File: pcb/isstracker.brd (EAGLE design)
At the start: 68.6 x 54.3 mm, 24 parts, among them IC2 L7805CV, J1 MOTOR_RIGHT, J2 MOTOR, J3 MOTOR_LEFT, J4 DISPLAY, J6 CONTROL, J8 UART, J9 DISTANCE, Q2 60V/32A/35mΩ, U1 ARGON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

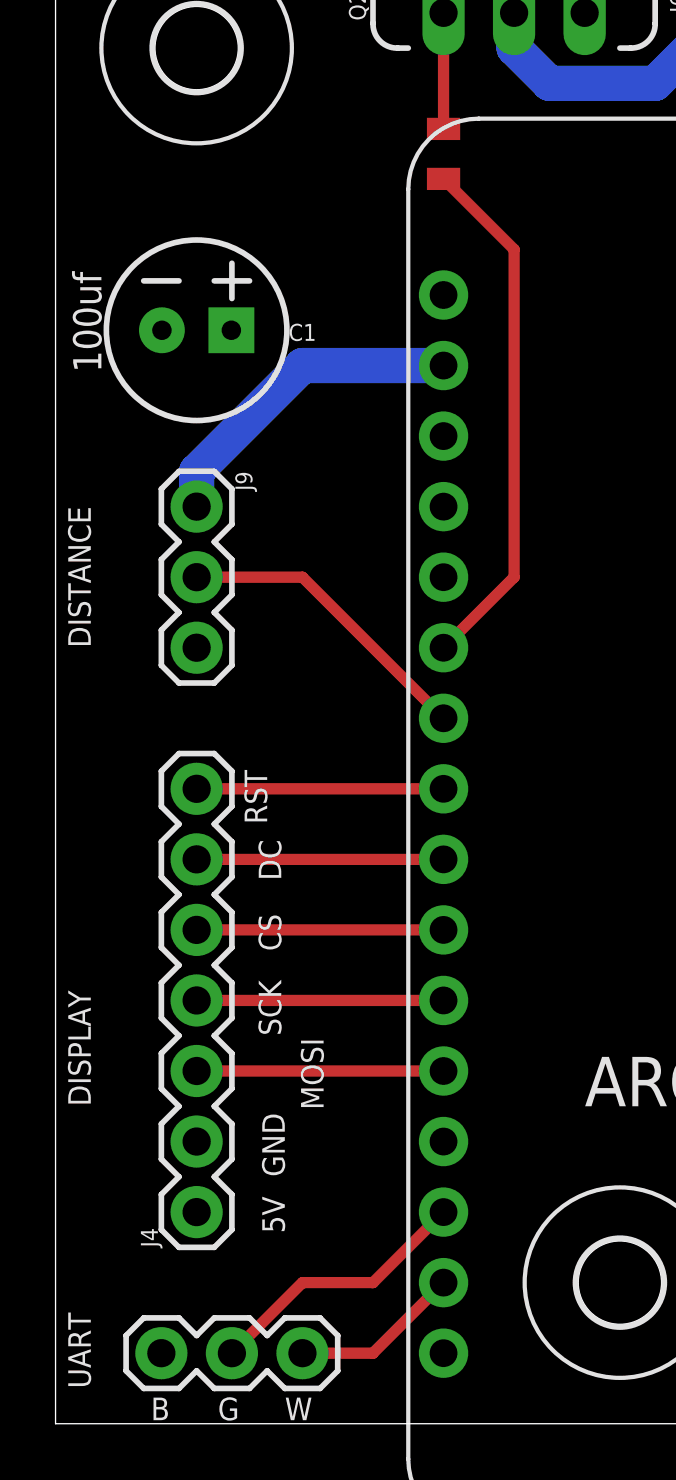
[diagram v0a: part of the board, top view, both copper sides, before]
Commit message: Control board version 1.7
* Added a pushbutton to turn the globe back on
* Began to put globe power control back into app
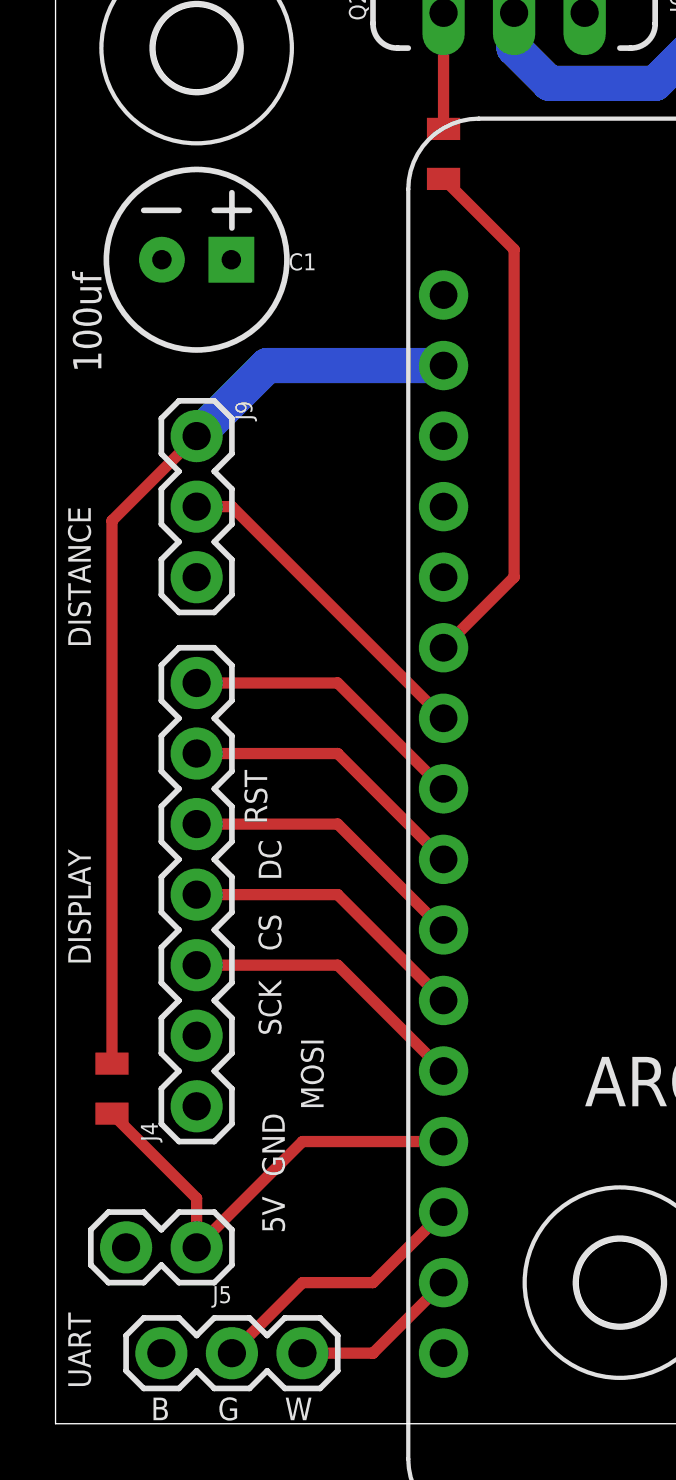
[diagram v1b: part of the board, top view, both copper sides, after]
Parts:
- added J5: GLOBE_RESET, SparkFun-Connectors:1X02
- added R4: 10k, SparkFun-Resistors:0805
- moved J4 3.81 mm to (5.08, 11.4)
- moved C1 2.54 mm to (5.08, 41.9)
- moved J9 2.54 mm to (5.08, 35.6)
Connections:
- new net MISO: J5.1, R4.2, U1.13
- net +3V3: now also R4.1
- net GND: now also J5.2
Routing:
- net +3V3: track 11.7 -> 33.8 mm
- net MISO: track 0.00 -> 16.5 mm
- net SCK: track 8.89 -> 10.5 mm
- net RST: track 8.89 -> 10.5 mm
- net MOSI: track 8.89 -> 10.5 mm
- net DC: track 8.89 -> 10.5 mm
- net CS: track 8.89 -> 10.5 mm
- net DISTANCE: track 11.0 -> 12.0 mm
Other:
- board text added: "ISS Position Tracker (C) Peter Buelow March, 2021 Version 1.7"
- board text removed: "ISS Position Tracker (C) Peter Buelow March, 2021 Version 1.6"
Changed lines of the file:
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@@
 <wire x1="68.56" y1="54.28" x2="0" y2="54.28" width="0" layer="20"/>
 <wire x1="0" y1="54.28" x2="0" y2="0" width="0" layer="20"/>
-<text x="1.27" y="11.43" size="0.8128" layer="121" rot="R90">DISPLAY</text>
+<text x="1.27" y="16.51" size="0.8128" layer="121" rot="R90">DISPLAY</text>
 <text x="33.147" y="48.514" size="0.8128" layer="121" rot="R180">CONTROL</text>
 <text x="27.686" y="53.721" size="0.6096" layer="121" rot="R180">GND</text>
@@
 (C) Peter Buelow
 March, 2021
-Version 1.6</text>
+Version 1.7</text>
 <text x="3.429" y="0.127" size="0.8128" layer="121">B</text>
 <text x="52.07" y="5.08" size="0.6096" layer="121">LM7805</text>
@@
 <attribute name="VALUE" x="52.578" y="49.53" size="0.6096" layer="27" font="vector" ratio="20" rot="R270"/>
 </element>
-<element name="J4" library="SparkFun-Connectors" library_urn="urn:adsk.eagle:library:513" package="1X07" package3d_urn="urn:adsk.eagle:package:38129/1" value="DISPLAY" x="5.08" y="7.62" smashed="yes" rot="R90">
-<attribute name="NAME" x="3.683" y="6.35" size="0.6096" layer="25" font="vector" ratio="20" rot="R90"/>
-</element>
-<element name="J9" library="SparkFun-Connectors" library_urn="urn:adsk.eagle:library:513" package="1X03" package3d_urn="urn:adsk.eagle:package:38063/1" value="DISTANCE" x="5.08" y="33.02" smashed="yes" rot="R270">
-<attribute name="NAME" x="6.477" y="34.29" size="0.6096" layer="25" font="vector" ratio="20" rot="R270"/>
+<element name="J4" library="SparkFun-Connectors" library_urn="urn:adsk.eagle:library:513" package="1X07" package3d_urn="urn:adsk.eagle:package:38129/1" value="DISPLAY" x="5.08" y="11.43" smashed="yes" rot="R90">
+<attribute name="NAME" x="3.683" y="10.16" size="0.6096" layer="25" font="vector" ratio="20" rot="R90"/>
+</element>
+<element name="J9" library="SparkFun-Connectors" library_urn="urn:adsk.eagle:library:513" package="1X03" package3d_urn="urn:adsk.eagle:package:38063/1" value="DISTANCE" x="5.08" y="35.56" smashed="yes" rot="R270">
+<attribute name="NAME" x="6.477" y="36.83" size="0.6096" layer="25" font="vector" ratio="20" rot="R270"/>
 </element>
 <element name="D1" library="diode" library_urn="urn:adsk.eagle:library:210" package="DO41-10" package3d_urn="urn:adsk.eagle:package:43336/1" value="1N4004" x="58.293" y="10.922" smashed="yes" rot="R270">
@@
 <attribute name="PROD_ID" value="CAP-08439" x="60.833" y="25.781" size="0.8128" layer="27" rot="R270" display="off"/>
 </element>
-<element name="C1" library="SparkFun-Capacitors" library_urn="urn:adsk.eagle:library:510" package="CPOL-RADIAL-2.5MM-6.5MM" package3d_urn="urn:adsk.eagle:package:37415/1" value="100uF" x="5.08" y="39.37" smashed="yes">
-<attribute name="NAME" x="8.89" y="38.989" size="0.6096" layer="25" font="vector" ratio="20" align="bottom-center"/>
-<attribute name="PROD_ID" value="CAP-08439" x="5.08" y="39.37" size="0.6096" layer="27" display="off"/>
+<element name="C1" library="SparkFun-Capacitors" library_urn="urn:adsk.eagle:library:510" package="CPOL-RADIAL-2.5MM-6.5MM" package3d_urn="urn:adsk.eagle:package:37415/1" value="100uF" x="5.08" y="41.91" smashed="yes">
+<attribute name="NAME" x="8.89" y="41.529" size="0.6096" layer="25" font="vector" ratio="20" align="bottom-center"/>
+<attribute name="PROD_ID" value="CAP-08439" x="5.08" y="41.91" size="0.6096" layer="27" display="off"/>
 </element>
 <element name="J3" library="SparkFun-Connectors" library_urn="urn:adsk.eagle:library:513" package="1X12" package3d_urn="urn:adsk.eagle:package:38169/1" value="MOTOR_LEFT" x="39.37" y="10.16" smashed="yes" rot="R90">
@@
 <element name="LED3" library="adafruit" library_urn="urn:adsk.eagle:library:420" package="CHIPLED_1206" package3d_urn="urn:adsk.eagle:package:6240560/1" value="L171L-LPGC" x="44.45" y="2.54" smashed="yes" rot="R90"/>
 <element name="LED1" library="adafruit" library_urn="urn:adsk.eagle:library:420" package="CHIPLED_1206" package3d_urn="urn:adsk.eagle:package:6240560/1" value="L171L-LPGC" x="35.56" y="48.26" smashed="yes" rot="R180"/>
+<element name="J5" library="SparkFun-Connectors" library_urn="urn:adsk.eagle:library:513" package="1X02" package3d_urn="urn:adsk.eagle:package:38039/1" value="GLOBE_RESET" x="5.08" y="6.35" smashed="yes" rot="R180">
+<attribute name="NAME" x="6.35" y="4.953" size="0.6096" layer="25" font="vector" ratio="20" rot="R180"/>
+<attribute name="VALUE" x="6.35" y="8.382" size="0.6096" layer="27" font="vector" ratio="20" rot="R180"/>
+</element>
+<element name="R4" library="SparkFun-Resistors" library_urn="urn:adsk.eagle:library:532" package="0805" package3d_urn="urn:adsk.eagle:package:39651/1" value="10k" x="2.032" y="12.065" smashed="yes" rot="R270">
+<attribute name="PROD_ID" value="RES-08474" x="2.032" y="12.065" size="0.8128" layer="27" rot="R270" display="off"/>
+<attribute name="VALUE" x="1.143" y="12.065" size="0.6096" layer="27" font="vector" ratio="20" rot="R270" align="top-center"/>
+</element>
 </elements>
 <signals>
@@
 <wire x1="39.37" y1="38.1" x2="35.56" y2="41.91" width="0.4064" layer="1"/>
 <wire x1="35.56" y1="41.91" x2="35.56" y2="46.51" width="0.4064" layer="1"/>
+<contactref element="J5" pad="2"/>
 </signal>
 <signal name="+5V">
@@
 <contactref element="U1" pad="12"/>
 <contactref element="J4" pad="3"/>
-<wire x1="5.08" y1="12.7" x2="13.97" y2="12.7" width="0.4064" layer="1"/>
+<wire x1="10.16" y1="16.51" x2="5.08" y2="16.51" width="0.4064" layer="1"/>
+<wire x1="10.16" y1="16.51" x2="13.97" y2="12.7" width="0.4064" layer="1"/>
 </signal>
 <signal name="SCK">
 <contactref element="U1" pad="11"/>
 <contactref element="J4" pad="4"/>
-<wire x1="5.08" y1="15.24" x2="13.97" y2="15.24" width="0.4064" layer="1"/>
+<wire x1="10.16" y1="19.05" x2="5.08" y2="19.05" width="0.4064" layer="1"/>
+<wire x1="10.16" y1="19.05" x2="13.97" y2="15.24" width="0.4064" layer="1"/>
 </signal>
 <signal name="RX">
@@
 <contactref element="U1" pad="10"/>
 <contactref element="J4" pad="5"/>
-<wire x1="5.08" y1="17.78" x2="13.97" y2="17.78" width="0.4064" layer="1"/>
+<wire x1="10.16" y1="21.59" x2="5.08" y2="21.59" width="0.4064" layer="1"/>
+<wire x1="10.16" y1="21.59" x2="13.97" y2="17.78" width="0.4064" layer="1"/>
 </signal>
 <signal name="DC">
 <contactref element="U1" pad="9"/>
 <contactref element="J4" pad="6"/>
-<wire x1="5.08" y1="20.32" x2="13.97" y2="20.32" width="0.4064" layer="1"/>
+<wire x1="10.16" y1="24.13" x2="5.08" y2="24.13" width="0.4064" layer="1"/>
+<wire x1="10.16" y1="24.13" x2="13.97" y2="20.32" width="0.4064" layer="1"/>
 </signal>
 <signal name="+3V3">
 <contactref element="U1" pad="2"/>
 <contactref element="J9" pad="1"/>
-<wire x1="13.97" y1="38.1" x2="8.89" y2="38.1" width="1.27" layer="16"/>
-<wire x1="8.89" y1="38.1" x2="5.08" y2="34.29" width="1.27" layer="16"/>
-<wire x1="5.08" y1="34.29" x2="5.08" y2="33.02" width="1.27" layer="16"/>
+<wire x1="13.97" y1="38.1" x2="7.62" y2="38.1" width="1.27" layer="16"/>
+<wire x1="7.62" y1="38.1" x2="5.08" y2="35.56" width="1.27" layer="16"/>
+<contactref element="R4" pad="1"/>
+<wire x1="5.08" y1="35.56" x2="2.032" y2="32.512" width="0.4064" layer="1"/>
+<wire x1="2.032" y1="32.512" x2="2.032" y2="12.965" width="0.4064" layer="1"/>
 </signal>
 <signal name="MTR_EN">
@@
 <contactref element="U1" pad="7"/>
 <contactref element="J9" pad="2"/>
-<wire x1="5.08" y1="30.48" x2="8.89" y2="30.48" width="0.4064" layer="1"/>
-<wire x1="8.89" y1="30.48" x2="13.97" y2="25.4" width="0.4064" layer="1"/>
+<wire x1="5.08" y1="33.02" x2="6.35" y2="33.02" width="0.4064" layer="1"/>
+<wire x1="6.35" y1="33.02" x2="13.97" y2="25.4" width="0.4064" layer="1"/>
 </signal>
 <signal name="RST">
 <contactref element="J4" pad="7"/>
 <contactref element="U1" pad="8"/>
-<wire x1="5.08" y1="22.86" x2="13.97" y2="22.86" width="0.4064" layer="1"/>
+<wire x1="10.16" y1="26.67" x2="13.97" y2="22.86" width="0.4064" layer="1"/>
+<wire x1="10.16" y1="26.67" x2="5.08" y2="26.67" width="0.4064" layer="1"/>
 </signal>
 <signal name="N$1">
@@
 <wire x1="16.51" y1="30.48" x2="16.51" y2="42.28" width="0.4064" layer="1"/>
 </signal>
+<signal name="MISO">
+<contactref element="U1" pad="13"/>
+<contactref element="J5" pad="1"/>
+<contactref element="R4" pad="2"/>
+<wire x1="5.08" y1="6.35" x2="8.89" y2="10.16" width="0.4064" layer="1"/>
+<wire x1="8.89" y1="10.16" x2="13.97" y2="10.16" width="0.4064" layer="1"/>
+<wire x1="2.032" y1="11.165" x2="5.08" y2="8.117" width="0.4064" layer="1"/>
+<wire x1="5.08" y1="8.117" x2="5.08" y2="6.35" width="0.4064" layer="1"/>
+</signal>
 </signals>

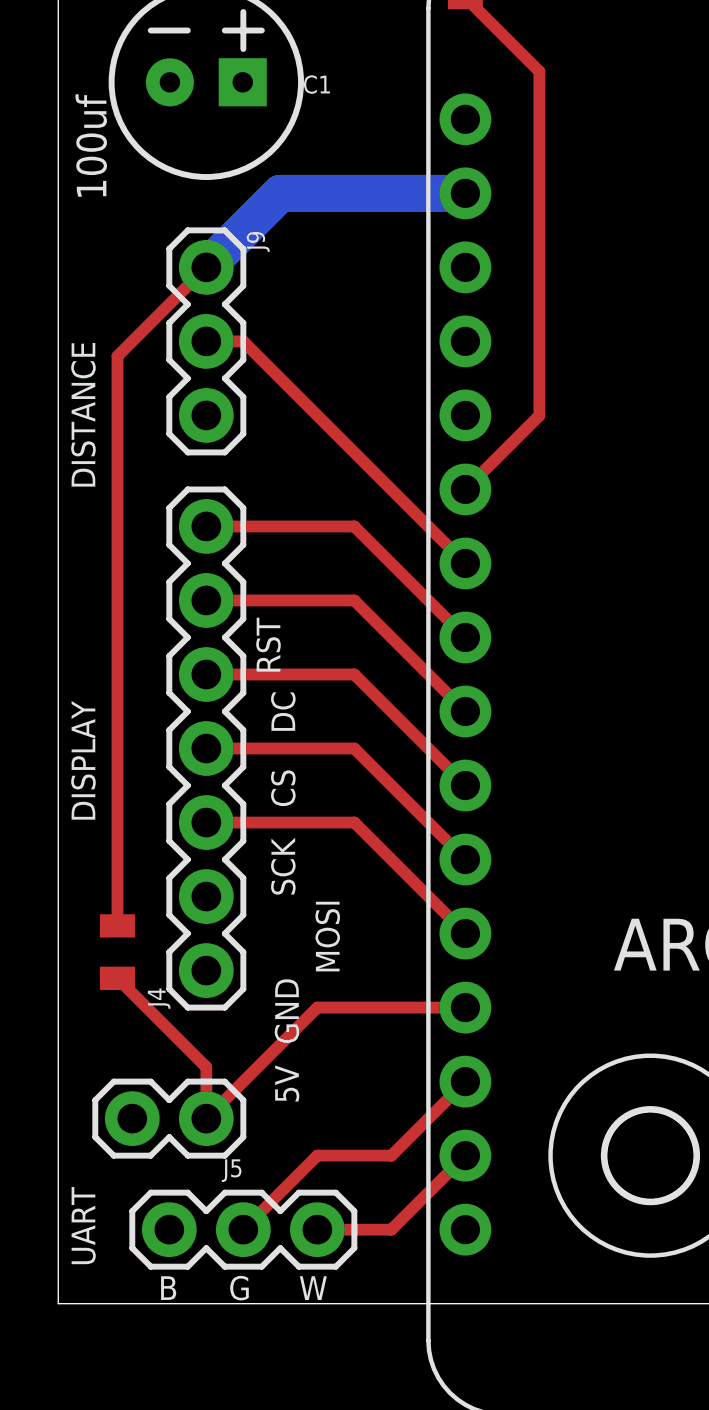
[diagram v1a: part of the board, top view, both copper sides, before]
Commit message: Bump control board revision
* Move pins around for display, motion, and pushbutton
* Add pushbutton
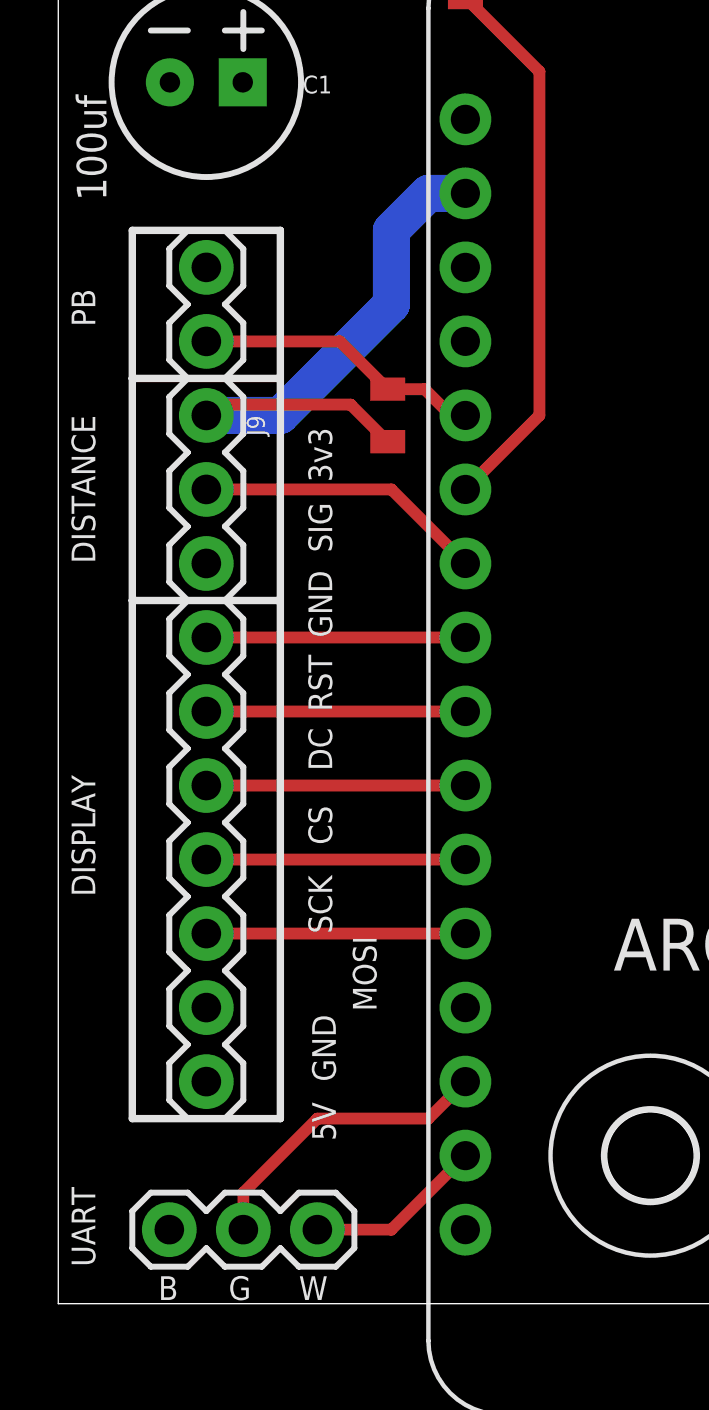
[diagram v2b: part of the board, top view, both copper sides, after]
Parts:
- moved J5 26.7 mm to (5.08, 33.0), turned to 90 degrees
- moved R4 20.6 mm to (11.3, 30.5), turned to 90 degrees
- moved J9 5.08 mm to (5.08, 30.5)
- moved J4 3.81 mm to (5.08, 7.62)
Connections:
- removed net MISO: J5.1, R4.2, U1.13
- new net GLOBE_EN: J5.1, R4.2, U1.5
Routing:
- net MISO: track 16.5 -> 0.00 mm
- net +3V3: track 33.8 -> 20.4 mm
- net GLOBE_EN: track 0.00 -> 9.94 mm
- net DISTANCE: track 12.0 -> 9.94 mm
- net SCK: track 10.5 -> 8.89 mm
- net RST: track 10.5 -> 8.89 mm
- net MOSI: track 10.5 -> 8.89 mm
- net DC: track 10.5 -> 8.89 mm
- net CS: track 10.5 -> 8.89 mm
- net RX: track 9.72 -> 10.5 mm
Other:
- board text added: "3v3"
- board text added: "ISS Position Tracker (C) Peter Buelow March, 2021 Version 1.8"
- board text added: "PB"
- board text added: "SIG"
- board text removed: "ISS Position Tracker (C) Peter Buelow March, 2021 Version 1.7"
